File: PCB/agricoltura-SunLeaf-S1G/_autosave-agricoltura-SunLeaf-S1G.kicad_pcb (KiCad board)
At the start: 4 copper layers, 100 x 40 mm, 125 parts, among them M1 SPSGRF-915, Q1 DMP3125L-7, Q2 DMP3125L-7, SW1 B3U-1000P, T1 BM04B-SRSS-TB(LF)(SN), T10 BM04B-SRSS-TB(LF)(SN), T11 BM04B-SRSS-TB(LF)(SN), T12 BM04B-SRSS-TB(LF)(SN), T13 BM04B-SRSS-TB(LF)(SN), T14 BM04B-SRSS-TB(LF)(SN), T15 BM04B-SRSS-TB(LF)(SN), T16 BM04B-SRSS-TB(LF)(SN), T17 BM04B-SRSS-TB(LF)(SN), T18 PPTC101LFBN-RC, T19 PPTC101LFBN-RC, T2 TC2050-IDC-NL-FP, T20 BU2032SM-JJ-GTR, T3 0475890001, T4 B2B-PH-K-S(LF)(SN), T5 B3B-PH-K-S(LF)(SN), T6 BM04B-SRSS-TB(LF)(SN), T7 BM04B-SRSS-TB(LF)(SN), T8 BM04B-SRSS-TB(LF)(SN), T9 BM04B-SRSS-TB(LF)(SN), U1 STM32F446RET6, U2 BQ24210DQCT, U3 AZ1117CR-3.3TRG1, U4 TCA9548APWR, U5 74HC4052D, U6 LTC2941CDCB-1#TRMPBF, X1 ABM3B-8.000MHZ-B2-T, X2 ABS07-32.768KHZ-9-T

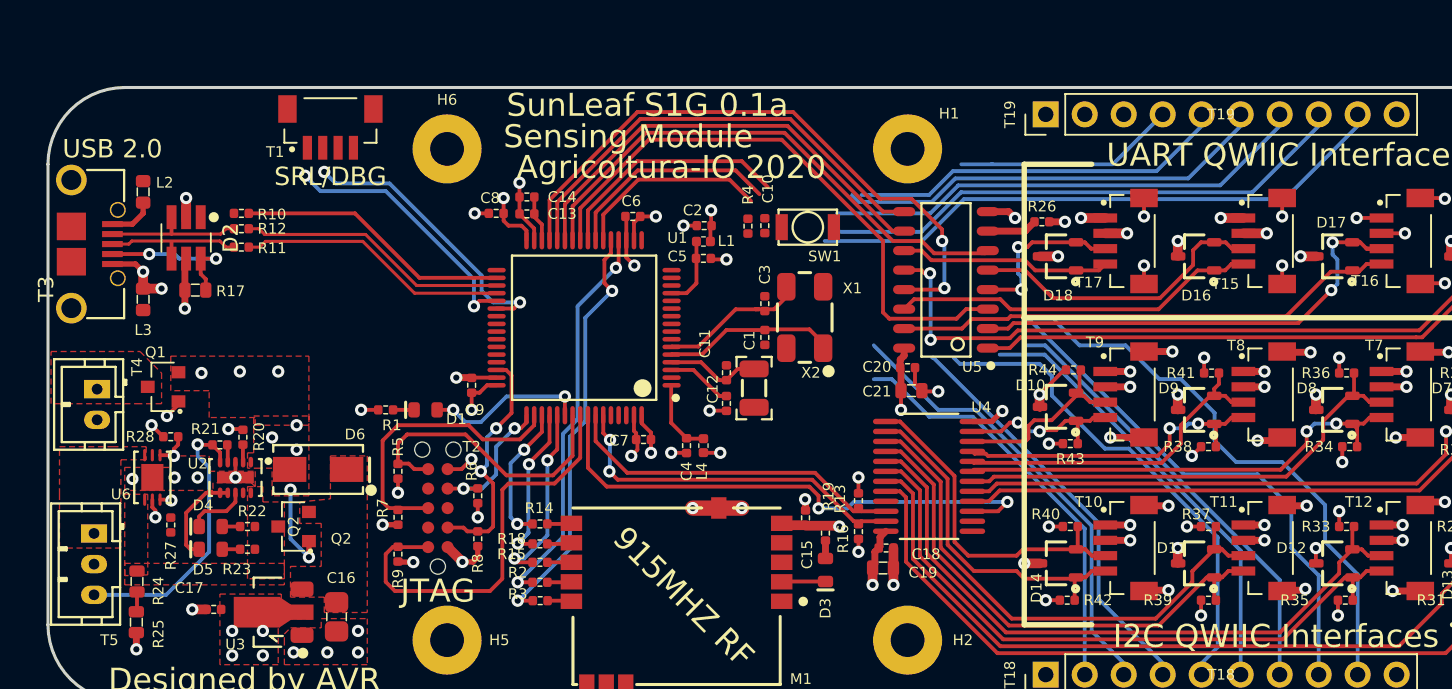
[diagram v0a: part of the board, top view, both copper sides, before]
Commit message: PCB Progress
PCB routing progress made, USB port replaced with micro b like older sunleaf designs.
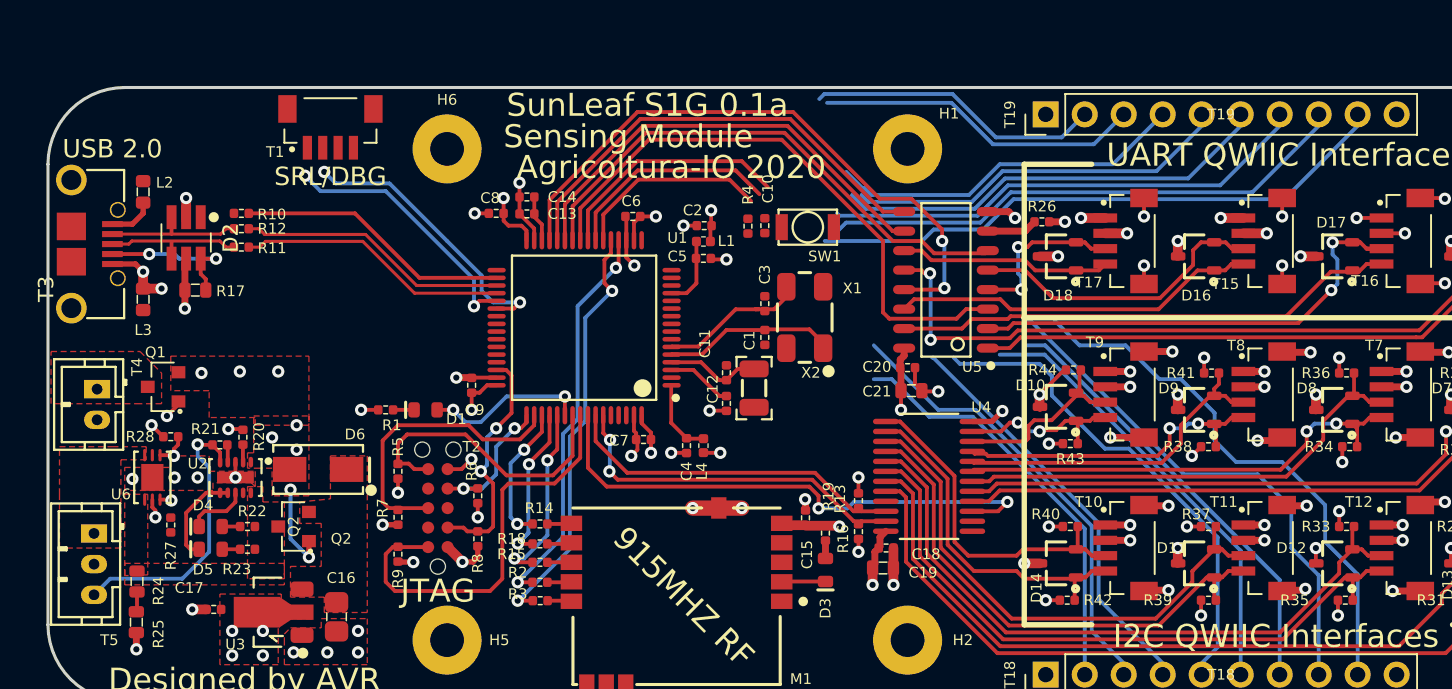
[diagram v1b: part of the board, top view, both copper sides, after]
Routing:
- net Net-(T19-Pad3): track 0.00 -> 21.3 mm
- net Net-(T19-Pad2): track 0.00 -> 19.2 mm
- net Net-(T19-Pad4): track 14.5 -> 23.4 mm
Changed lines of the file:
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@@
     (thickness 1.6)
     (drawings 56)
-    (tracks 1147)
+    (tracks 1166)
     (zones 0)
     (modules 125)
@@
   (segment (start 110.717 93.281926) (end 109.781926 93.281926) (width 0.25) (layer F.Cu) (net 49))
   (via (at 109.75 93.25) (size 0.8) (drill 0.4) (layers F.Cu B.Cu) (net 49))
+  (segment (start 103 103.05) (end 104.05 102) (width 0.25) (layer B.Cu) (net 49))
+  (segment (start 104.05 102) (end 108.75 102) (width 0.25) (layer B.Cu) (net 49))
+  (segment (start 108.75 102) (end 110.5 100.25) (width 0.25) (layer B.Cu) (net 49))
   (segment (start 109.75 94) (end 109.75 93.25) (width 0.25) (layer B.Cu) (net 49))
   (segment (start 110.5 94.75) (end 109.75 94) (width 0.25) (layer B.Cu) (net 49))
   (segment (start 110.5 100.25) (end 110.5 94.75) (width 0.25) (layer B.Cu) (net 49))
-  (segment (start 103 103.05) (end 107.7 103.05) (width 0.25) (layer B.Cu) (net 49))
-  (segment (start 107.7 103.05) (end 110.5 100.25) (width 0.25) (layer B.Cu) (net 49))
   (segment (start 161.225 79.356926) (end 163.660074 79.356926) (width 0.45) (layer F.Cu) (net 52))
   (segment (start 163.660074 79.356926) (end 164.267 78.75) (width 0.45) (layer F.Cu) (net 52))
@@
   (segment (start 178.8 95.2) (end 174 95.2) (width 0.25) (layer B.Cu) (net 117))
   (segment (start 174 95.2) (end 164 85.2) (width 0.25) (layer B.Cu) (net 117))
+  (segment (start 158.92501 70.42501) (end 150.57499 70.42501) (width 0.25) (layer B.Cu) (net 118))
+  (segment (start 161.75 73.25) (end 158.92501 70.42501) (width 0.25) (layer B.Cu) (net 118))
+  (segment (start 166.04 73.25) (end 161.75 73.25) (width 0.25) (layer B.Cu) (net 118))
+  (segment (start 150.57499 70.42501) (end 150.25 70.75) (width 0.25) (layer B.Cu) (net 118))
+  (segment (start 167.54 71.75) (end 166.04 73.25) (width 0.25) (layer B.Cu) (net 118))
+  (segment (start 161.5636 73.700011) (end 168.129989 73.700011) (width 0.25) (layer B.Cu) (net 119))
+  (segment (start 168.129989 73.700011) (end 170.08 71.75) (width 0.25) (layer B.Cu) (net 119))
+  (segment (start 150.75 71) (end 158.86359 71) (width 0.25) (layer B.Cu) (net 119))
+  (segment (start 158.86359 71) (end 161.5636 73.700011) (width 0.25) (layer B.Cu) (net 119))
+  (segment (start 153.049991 76.549991) (end 152 75.5) (width 0.25) (layer B.Cu) (net 120))
+  (segment (start 153.186401 76.549991) (end 153.049991 76.549991) (width 0.25) (layer B.Cu) (net 120))
+  (segment (start 169.37 75) (end 162 75) (width 0.25) (layer B.Cu) (net 120))
   (segment (start 172.62 71.75) (end 169.37 75) (width 0.25) (layer B.Cu) (net 120))
-  (segment (start 169.37 75) (end 161.5 75) (width 0.25) (layer B.Cu) (net 120))
-  (segment (start 161.5 75) (end 159.5 75) (width 0.25) (layer B.Cu) (net 120))
+  (segment (start 162 75) (end 160 77) (width 0.25) (layer B.Cu) (net 120))
+  (segment (start 160 77) (end 153.63641 77) (width 0.25) (layer B.Cu) (net 120))
+  (segment (start 153.63641 77) (end 153.186401 76.549991) (width 0.25) (layer B.Cu) (net 120))
+  (segment (start 160.186401 77.450009) (end 153.450009 77.450009) (width 0.25) (layer B.Cu) (net 121))
+  (segment (start 153.450009 77.450009) (end 153 77) (width 0.25) (layer B.Cu) (net 121))
+  (segment (start 162.186399 75.450011) (end 160.186401 77.450009) (width 0.25) (layer B.Cu) (net 121))
+  (segment (start 172.209989 75.450011) (end 162.186399 75.450011) (width 0.25) (layer B.Cu) (net 121))
   (segment (start 175.16 72.5) (end 172.209989 75.450011) (width 0.25) (layer B.Cu) (net 121))
-  (segment (start 172.209989 75.450011) (end 158.949989 75.450011) (width 0.25) (layer B.Cu) (net 121))
-  (segment (start 157.4 77) (end 153 77) (width 0.25) (layer B.Cu) (net 121))
-  (segment (start 158.949989 75.450011) (end 157.4 77) (width 0.25) (layer B.Cu) (net 121))
+  (segment (start 162.347866 75.924956) (end 160.372801 77.90002) (width 0.25) (layer B.Cu) (net 122))
+  (segment (start 160.372801 77.90002) (end 153.263609 77.90002) (width 0.25) (layer B.Cu) (net 122))
+  (segment (start 153.263609 77.90002) (end 152.4 77.036411) (width 0.25) (layer B.Cu) (net 122))
   (segment (start 152.4 77.036411) (end 152.4 77) (width 0.25) (layer B.Cu) (net 122))
-  (segment (start 152.8136 77.450011) (end 152.4 77.036411) (width 0.25) (layer B.Cu) (net 122))
-  (segment (start 174.275044 75.924956) (end 159.111453 75.924956) (width 0.25) (layer B.Cu) (net 122))
-  (segment (start 157.586399 77.450011) (end 152.8136 77.450011) (width 0.25) (layer B.Cu) (net 122))
+  (segment (start 174.275044 75.924956) (end 162.347866 75.924956) (width 0.25) (layer B.Cu) (net 122))
   (segment (start 177.7 72.5) (end 174.275044 75.924956) (width 0.25) (layer B.Cu) (net 122))
-  (segment (start 159.111453 75.924956) (end 157.586399 77.450011) (width 0.25) (layer B.Cu) (net 122))
-  (segment (start 176.365033 76.374967) (end 159.297853 76.374967) (width 0.25) (layer B.Cu) (net 123))
   (segment (start 180.24 72.5) (end 176.365033 76.374967) (width 0.25) (layer B.Cu) (net 123))
-  (segment (start 157.47282 78.2) (end 151.4 78.2) (width 0.25) (layer B.Cu) (net 123))
-  (segment (start 159.297853 76.374967) (end 157.47282 78.2) (width 0.25) (layer B.Cu) (net 123))
-  (segment (start 156.909231 79.4) (end 151.4 79.4) (width 0.25) (layer B.Cu) (net 124))
-  (segment (start 159.484253 76.824978) (end 156.909231 79.4) (width 0.25) (layer B.Cu) (net 124))
-  (segment (start 178.455022 76.824978) (end 159.484253 76.824978) (width 0.25) (layer B.Cu) (net 124))
+  (segment (start 151.550031 78.350031) (end 151.4 78.2) (width 0.25) (layer B.Cu) (net 123))
+  (segment (start 160.559201 78.350031) (end 151.550031 78.350031) (width 0.25) (layer B.Cu) (net 123))
+  (segment (start 162.534265 76.374967) (end 160.559201 78.350031) (width 0.25) (layer B.Cu) (net 123))
+  (segment (start 176.365033 76.374967) (end 162.534265 76.374967) (width 0.25) (layer B.Cu) (net 123))
+  (segment (start 178.455022 76.824978) (end 162.720664 76.824978) (width 0.25) (layer B.Cu) (net 124))
+  (segment (start 162.720664 76.824978) (end 160.745601 78.800042) (width 0.25) (layer B.Cu) (net 124))
+  (segment (start 160.745601 78.800042) (end 151.999958 78.800042) (width 0.25) (layer B.Cu) (net 124))
   (segment (start 182.78 72.5) (end 178.455022 76.824978) (width 0.25) (layer B.Cu) (net 124))
+  (segment (start 151.999958 78.800042) (end 151.4 79.4) (width 0.25) (layer B.Cu) (net 124))
   (segment (start 167.2 86.8) (end 165.6 85.2) (width 0.25) (layer B.Cu) (net 125))
   (segment (start 170.2 86.8) (end 167.2 86.8) (width 0.25) (layer B.Cu) (net 125))
@@
   (segment (start 183.2 97.2) (end 180.4 94.4) (width 0.25) (layer B.Cu) (net 125))
   (segment (start 176 93) (end 176 91.2) (width 0.25) (layer B.Cu) (net 125))
-  (segment (start 185.32 72.5) (end 180.545019 77.274981) (width 0.25) (layer B.Cu) (net 126))
-  (segment (start 180.545019 77.274981) (end 159.670661 77.274981) (width 0.25) (layer B.Cu) (net 126))
   (segment (start 156.945642 80) (end 150.6 80) (width 0.25) (layer B.Cu) (net 126))
-  (segment (start 159.670661 77.274981) (end 156.945642 80) (width 0.25) (layer B.Cu) (net 126))
+  (segment (start 162.907064 77.274989) (end 160.932001 79.250053) (width 0.25) (layer B.Cu) (net 126))
+  (segment (start 160.932001 79.250053) (end 157.695589 79.250053) (width 0.25) (layer B.Cu) (net 126))
+  (segment (start 180.545011 77.274989) (end 162.907064 77.274989) (width 0.25) (layer B.Cu) (net 126))
+  (segment (start 185.32 72.5) (end 180.545011 77.274989) (width 0.25) (layer B.Cu) (net 126))
+  (segment (start 157.695589 79.250053) (end 156.945642 80) (width 0.25) (layer B.Cu) (net 126))
   (segment (start 196 106) (end 192.7 109.3) (width 0.635) (layer In1.Cu) (net 127))
   (segment (start 158.3 109.3) (end 155 106) (width 0.635) (layer In1.Cu) (net 127))
@@
       (pts
         (xy 200 110) (xy 148.8 109.8) (xy 148.8 96.5) (xy 133.2 96.5) (xy 133.2 110)
-        (xy 111 110) (xy 111 103.4) (xy 117 103.4) (xy 117 102.6) (xy 117 93.75)
-        (xy 117 87.25) (xy 114.25 87.25) (xy 114 70) (xy 200 70)
+        (xy 98.75 110) (xy 98.75 103.4) (xy 117 103.4) (xy 117 102.6) (xy 117 93.75)
+        (xy 117 87.25) (xy 114.25 87.25) (xy 114.25 70) (xy 200 70)
       )
     )
@@
     (polygon
       (pts
-        (xy 113.5 87.5) (xy 116.8 87.5) (xy 116.8 96.75) (xy 106.5 96.75) (xy 106.5 75)
+        (xy 113.5 87.5) (xy 116.8 87.5) (xy 116.8 96.75) (xy 107.5 96.75) (xy 107.5 75)
         (xy 113.5 75)
       )
